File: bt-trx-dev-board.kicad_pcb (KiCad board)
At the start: 2 copper layers, 64.5 x 68 mm, 53 parts, among them J2 PTT_BUTTON, J3 AudioJack2, J4 PTT_SELECT, J5 RJ45, J6 ENABLE_PTT_IN, J7 I2C, SW1 SW_Push, U1 SILabs_WT32i, U2 LM1117-5.0, U3 Teensy3.2

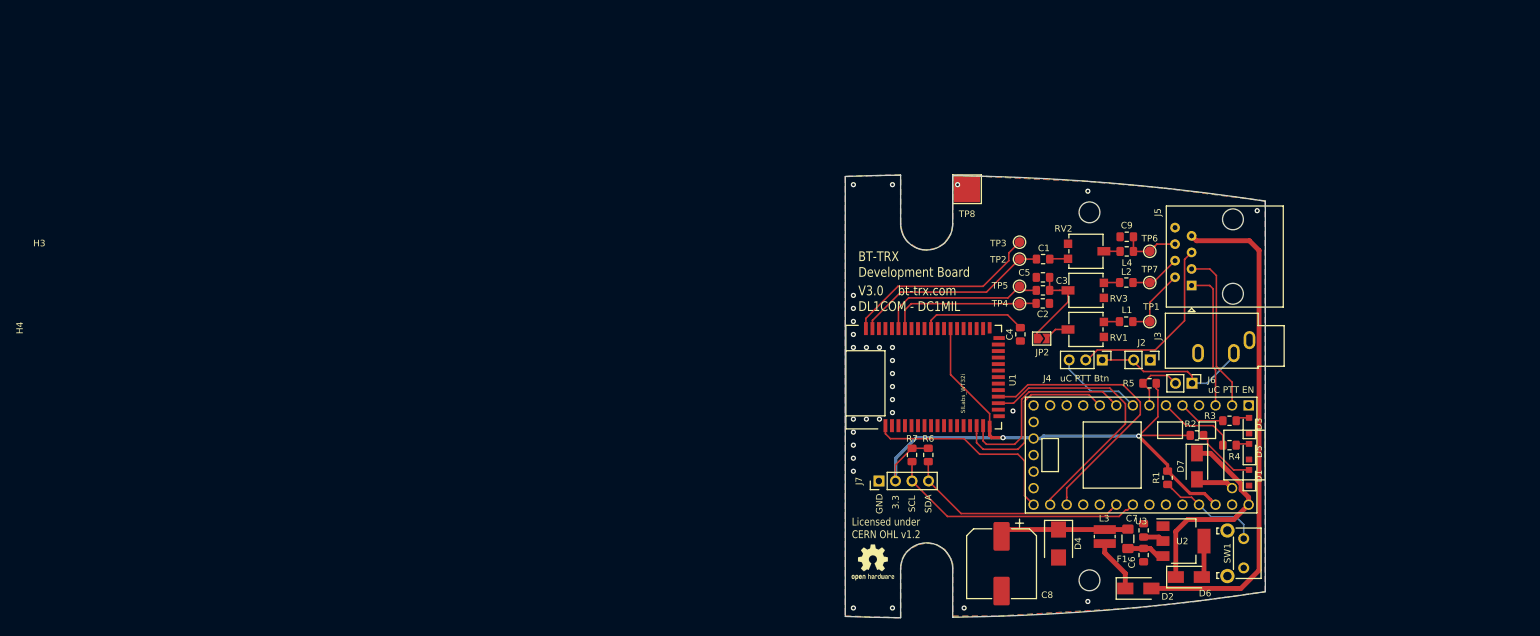
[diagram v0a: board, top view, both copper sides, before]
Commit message: Continued v4 [#1]
*removed all v3 stuff
* Resized board to max case size
* First deratsnesting
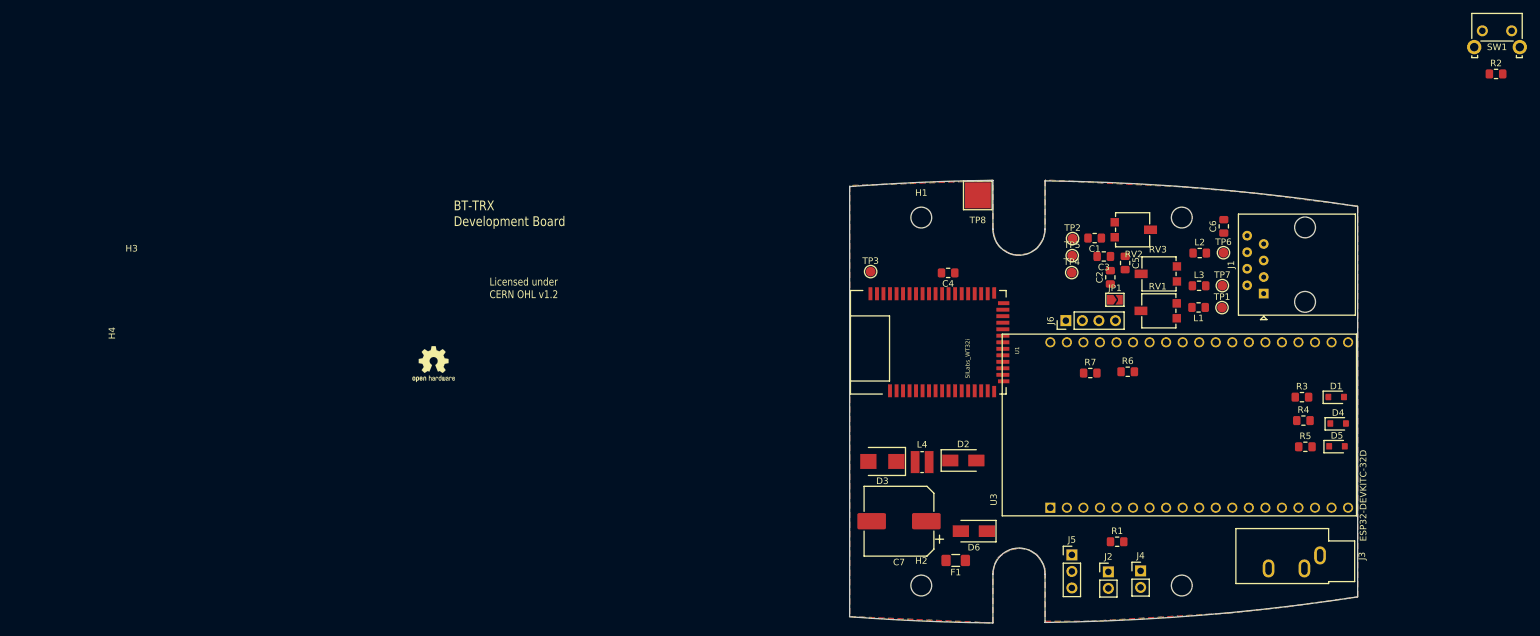
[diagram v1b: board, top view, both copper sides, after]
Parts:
- removed C8: 220uF, Capacitor_SMD:CP_Elec_10x10.5
- removed C9: 10nF, Capacitor_SMD:C_0805_2012Metric_Pad1.15x1.40mm_HandSolder
- removed D7: 1N5817, Diode_SMD:D_SMA
- removed J7: I2C, Connector_PinHeader_2.54mm:PinHeader_1x04_P2.54mm_Vertical
- removed JP2: AUDIO_B, Jumper:SolderJumper-2_P1.3mm_Open_TrianglePad1.0x1.5mm
- removed U2: LM1117-5.0, Package_TO_SOT_SMD:SOT-223-3_TabPin2
- added H1: MountingHole, MountingHole:MountingHole_3.2mm_M3_DIN965, F.Cu at (131.4, 71.0)
- added H2: MountingHole, MountingHole:MountingHole_3.2mm_M3_DIN965, F.Cu at (131.4, 127.5)
- added J1: RJ45, Connector_RJ:RJ45_Amphenol_54602-x08_Horizontal, F.Cu at (184.0, 82.7)
- added JP1: AUDIO_B, Jumper:SolderJumper-2_P1.3mm_Open_TrianglePad1.0x1.5mm, F.Cu at (161.2, 83.7)
- C6: value 100nF tantal -> 10nF
- C7: value 100nF tantal -> 220uF 25V; footprint Capacitor_SMD:C_0805_2012Metric_Pad1.15x1.40mm_HandSolder -> Capacitor_SMD:CP_Elec_10x10.5
- D3: value LED BLUE 2mA -> TVS 16V; footprint Kingbright:APA2107LSECK -> Diode_SMD:D_SMB
- D4: value TVS 16V -> LED BLUE 2mA; footprint Diode_SMD:D_SMB -> Kingbright:APA2107LSECK
- J4: value PTT_SELECT -> ENABLE_PTT_IN; footprint Connector_PinHeader_2.54mm:PinHeader_1x03_P2.54mm_Vertical -> Connector_PinHeader_2.54mm:PinHeader_1x02_P2.54mm_Vertical
- J5: value RJ45 -> PTT_SELECT; footprint Connector_RJ:RJ45_Amphenol_54602-x08_Horizontal -> Connector_PinHeader_2.54mm:PinHeader_1x03_P2.54mm_Vertical
- J6: value ENABLE_PTT_IN -> I2C; footprint Connector_PinHeader_2.54mm:PinHeader_1x02_P2.54mm_Vertical -> Connector_PinHeader_2.54mm:PinHeader_1x04_P2.54mm_Vertical
- L3: value 47uH, 390mA -> 100nH; footprint Inductor_SMD:L_Wuerth_MAPI-3020 -> Inductor_SMD:L_0805_2012Metric_Pad1.15x1.40mm_HandSolder
- L4: value 100nH -> 47uH, 390mA; footprint Inductor_SMD:L_0805_2012Metric_Pad1.15x1.40mm_HandSolder -> Inductor_SMD:L_Wuerth_MAPI-3020
- R2: value 2.2k -> 10k
- R3: value 820R -> 2.2k
- R5: value 10k -> 820R
- U3: value Teensy3.2 -> ESP32-DEVKITC-32D; footprint teensy:Teensy30_31_32_LC_stripped -> ESP32-DEVKITC-32D:MODULE_ESP32-DEVKITC-32D
- moved SW1 86.2 mm to (217.6, 42.4), turned to 0 degrees
- moved N1 74.0 mm to (56.5, 93.5)
- moved R2 72.0 mm to (219.7, 49.0)
- moved D3 56.6 mm to (125.5, 108.5), turned to 180 degrees
- moved C6 52.0 mm to (177.9, 72.4), turned to 90 degrees
- moved D4 46.7 mm to (195.4, 102.7), turned to 0 degrees
- moved J5 45.3 mm to (154.6, 122.8), turned to 0 degrees
- moved L4 45.1 mm to (131.6, 108.6)
- moved L3 41.1 mm to (174.1, 81.5), turned to 0 degrees
- moved C7 37.6 mm to (128.0, 117.7), turned to 180 degrees
- moved J3 34.8 mm to (192.7, 122.9)
- moved D6 33.7 mm to (139.5, 119.2), turned to 180 degrees
- moved D2 33.3 mm to (137.9, 108.3)
- moved R6 33.2 mm to (163.1, 94.7), turned to 0 degrees
- moved J2 33.2 mm to (160.2, 125.5), turned to 0 degrees
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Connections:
- C6 pad 1: Net-(C6-Pad1) -> /AUDIO_OUT
- D3 pad 1: GND -> Net-(C7-Pad1)
- D3 pad 2: Net-(D3-Pad2) -> GND
- D4 pad 1: Net-(C8-Pad1) -> GND
- D4 pad 2: GND -> Net-(D4-Pad2)
- D6 pad 2: Net-(C7-Pad1) -> Net-(D6-Pad2)
- F1 pad 1: Net-(C6-Pad1) -> Net-(D6-Pad2)
- F1 pad 2: Net-(C8-Pad1) -> Net-(C7-Pad1)
- J4 pad 2: /PTT -> /UC_PTT_IN
- J5 pad 1: /CAT_TX -> /PTT_BUTTON
- J5 pad 2: /AUDIO_IN_B -> /PTT
- J5 pad 3: /CAT_RX -> /UC_PTT_OUT
- J6 pad 1: /PTT_BUTTON -> GND
- J6 pad 2: /PTT_IN -> +3V3
- L2 pad 2: /AUDIO_IN_A -> /AUDIO_OUT
- L3 pad 1: Net-(C8-Pad1) -> Net-(L3-Pad1)
- L3 pad 2: Net-(D2-Pad1) -> /AUDIO_IN_A
- L4 pad 1: Net-(L4-Pad1) -> Net-(C7-Pad1)
- L4 pad 2: /AUDIO_OUT -> Net-(D2-Pad1)
- R1 pad 2: /Microcontroller/BTN0 -> /UC_PTT_IN
- R2 pad 2: Net-(D1-Pad2) -> /Microcontroller/BTN0
- R3 pad 1: /Microcontroller/LED0 -> +3V3
- R3 pad 2: Net-(D3-Pad2) -> Net-(D1-Pad2)
- R4 pad 1: /Microcontroller/LED1 -> /Microcontroller/LED0
- R4 pad 2: Net-(D5-Pad2) -> Net-(D4-Pad2)
- R5 pad 1: +3V3 -> /Microcontroller/LED1
- R5 pad 2: /PTT_IN -> Net-(D5-Pad2)
- RV2 pad 2: Net-(L4-Pad1) -> Net-(L2-Pad1)
- RV3 pad 1: Net-(L2-Pad1) -> Net-(L3-Pad1)
- U3 pad 1: GND -> +3V3
- U3 pad 10: /UART_UC_TX -> /Microcontroller/LED1
- U3 pad 14: (no net) -> GND
- U3 pad 16: +3V3 -> (no net)
- U3 pad 17: GND -> (no net)
- U3 pad 19: (no net) -> +5V
- U3 pad 2: /CAT_RX -> (no net)
- U3 pad 20: /WT32_ONOFF_FROM_UC -> GND
- U3 pad 21: /UART_UC_CTS -> /WT32_ONOFF_FROM_UC
- U3 pad 22: /UART_UC_RTS -> /Microcontroller/SCL
- U3 pad 26: /Microcontroller/SCL -> GND
- U3 pad 28: (no net) -> /UART_UC_CTS
- U3 pad 29: (no net) -> /UART_UC_RTS
- U3 pad 3: /CAT_TX -> (no net)
- U3 pad 30: /Microcontroller/BTN0 -> /UART_UC_TX
- U3 pad 31: +3V3 -> /UART_UC_RX
- U3 pad 32: GND -> /Microcontroller/BTN0
- U3 pad 33: +5V -> (no net)
- U3 pad 34: /Microcontroller/VUSB -> (no net)
- U3 pad 5: /Microcontroller/LED0 -> (no net)
- U3 pad 6: /Microcontroller/LED1 -> (no net)
- U3 pad 7: /PTT_IN -> /UC_PTT_IN
- U3 pad 8: /PTT_UC -> /UC_PTT_OUT
- U3 pad 9: /UART_UC_RX -> /Microcontroller/LED0
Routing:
- net +3V3: track 106.1 -> 0.00 mm, vias 2 -> 0
- net /V_IN: track 78.1 -> 0.00 mm
- net /UART_UC_RTS: track 44.1 -> 0.00 mm
- net /UART_UC_CTS: track 41.8 -> 0.00 mm
- net /Microcontroller/SCL: track 39.9 -> 0.00 mm
- net /Microcontroller/SDA: track 34.5 -> 0.00 mm
- net +5V: track 32.3 -> 0.00 mm
- net /WT32_ONOFF_FROM_UC: track 31.6 -> 0.00 mm
- net /SPK_LP: track 30.7 -> 0.00 mm
- net /UART_UC_RX: track 30.7 -> 0.00 mm
- net /SPK_LN: track 30.3 -> 0.00 mm
- net /UART_UC_TX: track 29.8 -> 0.00 mm
- net /PTT: track 28.7 -> 0.00 mm
- net /MIC_LN: track 25.9 -> 0.00 mm
- net /CAT_RX: track 25.2 -> 0.00 mm
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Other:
- board size 64.5 x 68 mm -> 78 x 68 mm
- board text removed: "3.3"
- board text removed: "GND"
- board text removed: "SCL"
- board text removed: "SDA"
- board text removed: "V3.0 bt-trx.com DL1COM - DC1MIL"
- board text removed: "uC PTT Btn"
- board text removed: "uC PTT EN"

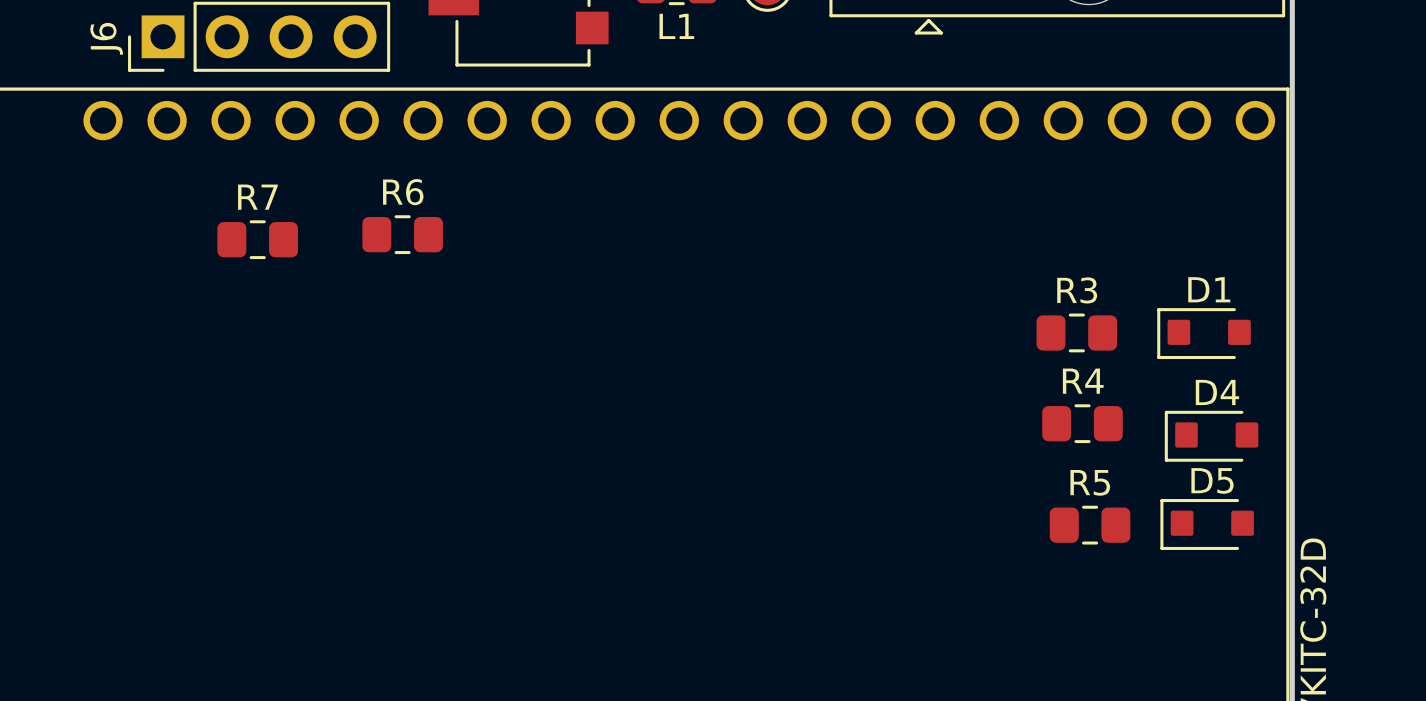
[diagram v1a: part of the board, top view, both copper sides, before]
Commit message: [#1] Refined Schematic
* Removed RTS CTS
* Added 15pF capacitator to audio IN+
* Removed PTT jumper
* Added pull-up jumper
* Added solder jmpr bypass to RV
* Changed button footprint to SMD version
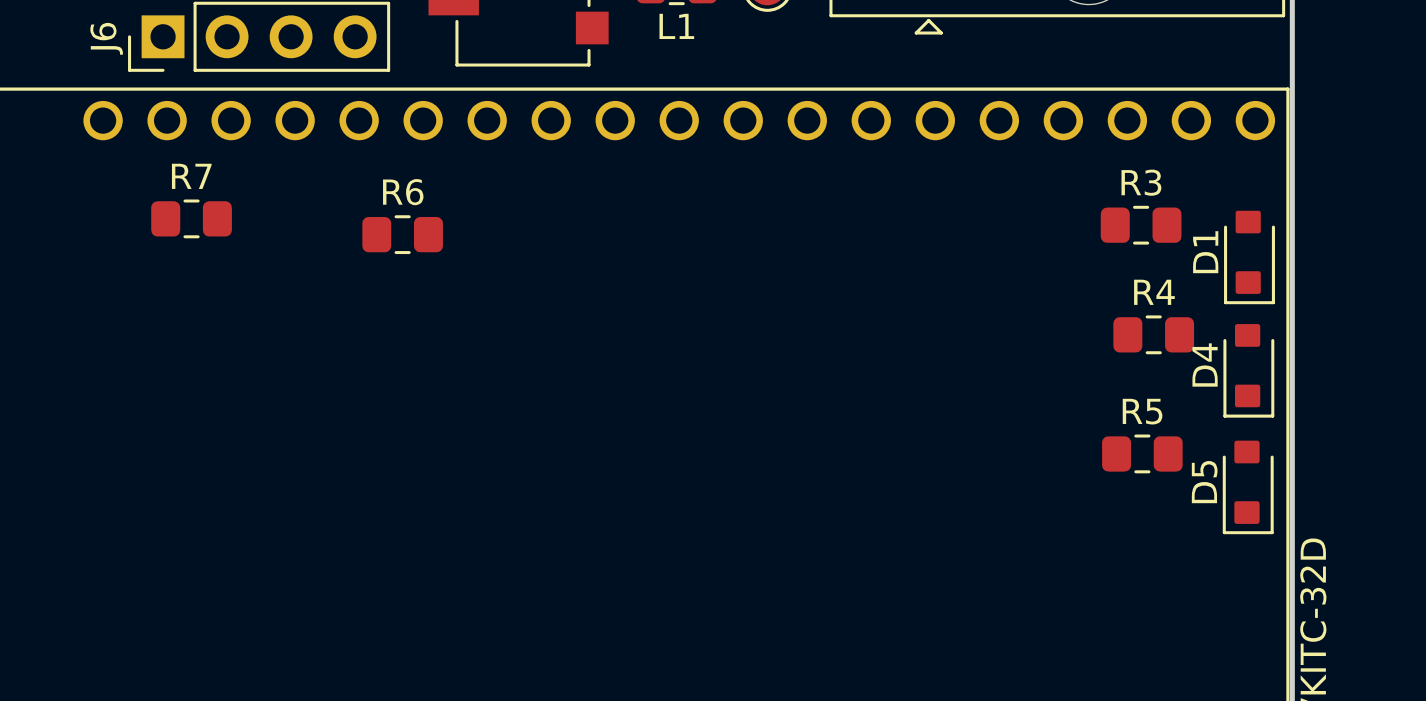
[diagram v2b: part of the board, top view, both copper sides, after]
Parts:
- moved R3 4.98 mm to (192.4, 94.3)
- moved R4 4.52 mm to (192.9, 98.7)
- moved D1 3.53 mm to (196.7, 95.4), turned to 90 degrees
- moved R5 3.51 mm to (192.5, 103.4)
- moved D4 3.01 mm to (196.7, 99.9), turned to 90 degrees
- moved R7 2.75 mm to (154.8, 94.1)
- moved D5 2.13 mm to (196.6, 104.5), turned to 90 degrees
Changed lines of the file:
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@@
   )
   (module Kingbright:APA2107LSECK (layer F.Cu)
-    (at 195.125 98.6)
+    (at 196.675 95.425 90)
     (descr "LED SMD 0805 (2012 Metric), square (rectangular) end terminal, IPC_7351 nominal, (Body size source: https://docs.google.com/spreadsheets/d/1BsfQQcO9C6DZCsRaXUlFlo91Tg2WpOkGARC1WS5S8t0/edit?usp=sharing), generated with kicad-footprint-generator")
     (tags diode)
     (attr smd)
-    (fp_text reference D1 (at 0 -1.65) (layer F.SilkS)
-      (effects (font (size 1 1) (thickness 0.15)))
-    )
-    (fp_text value "LED AMBER 2mA" (at 0 1.8) (layer F.Fab)
+    (fp_text reference D1 (at 0 -1.65 90) (layer F.SilkS)
+      (effects (font (size 1 1) (thickness 0.15)))
+    )
+    (fp_text value "LED AMBER 2mA" (at 0 1.8 90) (layer F.Fab)
       (effects (font (size 1 1) (thickness 0.15)))
     )
@@
     (fp_line (start 2 -0.9) (end 2 1) (layer F.CrtYd) (width 0.05))
     (fp_line (start 2 1) (end -2 1) (layer F.CrtYd) (width 0.05))
-    (fp_text user %R (at 0 0) (layer F.Fab)
+    (fp_text user %R (at 0 0 90) (layer F.Fab)
       (effects (font (size 0.5 0.5) (thickness 0.08)))
     )
-    (pad 1 smd roundrect (at -1.2 0) (size 0.9 1) (layers F.Cu F.Paste F.Mask) (roundrect_rratio 0.1)
-      (net 1 GND))
-    (pad 2 smd roundrect (at 1.2 0) (size 0.9 1) (layers F.Cu F.Paste F.Mask) (roundrect_rratio 0.1)
+    (pad 1 smd roundrect (at -1.2 0 90) (size 0.9 1) (layers F.Cu F.Paste F.Mask) (roundrect_rratio 0.1)
+      (net 1 GND))
+    (pad 2 smd roundrect (at 1.2 0 90) (size 0.9 1) (layers F.Cu F.Paste F.Mask) (roundrect_rratio 0.1)
       (net 29 "Net-(D1-Pad2)"))
     (model ${KISYS3DMOD}/LED_SMD.3dshapes/LED_0805_2012Metric.wrl
@@
   )
   (module Kingbright:APA2107LSECK (layer F.Cu)
-    (at 195.425 102.675)
+    (at 196.65 99.925 90)
     (descr "LED SMD 0805 (2012 Metric), square (rectangular) end terminal, IPC_7351 nominal, (Body size source: https://docs.google.com/spreadsheets/d/1BsfQQcO9C6DZCsRaXUlFlo91Tg2WpOkGARC1WS5S8t0/edit?usp=sharing), generated with kicad-footprint-generator")
     (tags diode)
     (attr smd)
-    (fp_text reference D4 (at 0 -1.65) (layer F.SilkS)
-      (effects (font (size 1 1) (thickness 0.15)))
-    )
-    (fp_text value "LED BLUE 2mA" (at 0 1.8) (layer F.Fab)
+    (fp_text reference D4 (at 0 -1.65 90) (layer F.SilkS)
+      (effects (font (size 1 1) (thickness 0.15)))
+    )
+    (fp_text value "LED BLUE 2mA" (at 0 1.8 90) (layer F.Fab)
       (effects (font (size 1 1) (thickness 0.15)))
     )
@@
     (fp_line (start 2 -0.9) (end 2 1) (layer F.CrtYd) (width 0.05))
     (fp_line (start 2 1) (end -2 1) (layer F.CrtYd) (width 0.05))
-    (fp_text user %R (at 0 0) (layer F.Fab)
+    (fp_text user %R (at 0 0 90) (layer F.Fab)
       (effects (font (size 0.5 0.5) (thickness 0.08)))
     )
-    (pad 1 smd roundrect (at -1.2 0) (size 0.9 1) (layers F.Cu F.Paste F.Mask) (roundrect_rratio 0.1)
-      (net 1 GND))
-    (pad 2 smd roundrect (at 1.2 0) (size 0.9 1) (layers F.Cu F.Paste F.Mask) (roundrect_rratio 0.1)
+    (pad 1 smd roundrect (at -1.2 0 90) (size 0.9 1) (layers F.Cu F.Paste F.Mask) (roundrect_rratio 0.1)
+      (net 1 GND))
+    (pad 2 smd roundrect (at 1.2 0 90) (size 0.9 1) (layers F.Cu F.Paste F.Mask) (roundrect_rratio 0.1)
       (net 33 "Net-(D4-Pad2)"))
     (model ${KISYS3DMOD}/LED_SMD.3dshapes/LED_0805_2012Metric.wrl
@@
   )
   (module Kingbright:APA2107LSECK (layer F.Cu)
-    (at 195.25 106.175)
+    (at 196.625 104.55 90)
     (descr "LED SMD 0805 (2012 Metric), square (rectangular) end terminal, IPC_7351 nominal, (Body size source: https://docs.google.com/spreadsheets/d/1BsfQQcO9C6DZCsRaXUlFlo91Tg2WpOkGARC1WS5S8t0/edit?usp=sharing), generated with kicad-footprint-generator")
     (tags diode)
     (attr smd)
-    (fp_text reference D5 (at 0 -1.65) (layer F.SilkS)
-      (effects (font (size 1 1) (thickness 0.15)))
-    )
-    (fp_text value "LED GREEN 2mA" (at 0 1.8) (layer F.Fab)
-      (effects (font (size 1 1) (thickness 0.15)))
-    )
-    (fp_text user %R (at 0 0) (layer F.Fab)
+    (fp_text reference D5 (at 0 -1.65 90) (layer F.SilkS)
+      (effects (font (size 1 1) (thickness 0.15)))
+    )
+    (fp_text value "LED GREEN 2mA" (at 0 1.8 90) (layer F.Fab)
+      (effects (font (size 1 1) (thickness 0.15)))
+    )
+    (fp_text user %R (at 0 0 90) (layer F.Fab)
       (effects (font (size 0.5 0.5) (thickness 0.08)))
     )
@@
     (fp_line (start -0.7 -0.6) (end -1 -0.3) (layer F.Fab) (width 0.1))
     (fp_line (start 1 -0.6) (end -0.7 -0.6) (layer F.Fab) (width 0.1))
-    (pad 2 smd roundrect (at 1.2 0) (size 0.9 1) (layers F.Cu F.Paste F.Mask) (roundrect_rratio 0.1)
+    (pad 2 smd roundrect (at 1.2 0 90) (size 0.9 1) (layers F.Cu F.Paste F.Mask) (roundrect_rratio 0.1)
       (net 27 "Net-(D5-Pad2)"))
-    (pad 1 smd roundrect (at -1.2 0) (size 0.9 1) (layers F.Cu F.Paste F.Mask) (roundrect_rratio 0.1)
+    (pad 1 smd roundrect (at -1.2 0 90) (size 0.9 1) (layers F.Cu F.Paste F.Mask) (roundrect_rratio 0.1)
       (net 1 GND))
     (model ${KISYS3DMOD}/LED_SMD.3dshapes/LED_0805_2012Metric.wrl
@@
   )
   (module Resistor_SMD:R_0805_2012Metric_Pad1.15x1.40mm_HandSolder (layer F.Cu)
-    (at 189.875 98.625)
+    (at 192.425 94.35)
     (descr "Resistor SMD 0805 (2012 Metric), square (rectangular) end terminal, IPC_7351 nominal with elongated pad for handsoldering. (Body size source: https://docs.google.com/spreadsheets/d/1BsfQQcO9C6DZCsRaXUlFlo91Tg2WpOkGARC1WS5S8t0/edit?usp=sharing), generated with kicad-footprint-generator")
     (tags "resistor handsolder")
@@
   )
   (module Resistor_SMD:R_0805_2012Metric_Pad1.15x1.40mm_HandSolder (layer F.Cu)
-    (at 190.1 102.225)
+    (at 192.925 98.7)
     (descr "Resistor SMD 0805 (2012 Metric), square (rectangular) end terminal, IPC_7351 nominal with elongated pad for handsoldering. (Body size source: https://docs.google.com/spreadsheets/d/1BsfQQcO9C6DZCsRaXUlFlo91Tg2WpOkGARC1WS5S8t0/edit?usp=sharing), generated with kicad-footprint-generator")
     (tags "resistor handsolder")
@@
   )
   (module Resistor_SMD:R_0805_2012Metric_Pad1.15x1.40mm_HandSolder (layer F.Cu)
-    (at 190.4 106.25)
+    (at 192.475 103.425)
     (descr "Resistor SMD 0805 (2012 Metric), square (rectangular) end terminal, IPC_7351 nominal with elongated pad for handsoldering. (Body size source: https://docs.google.com/spreadsheets/d/1BsfQQcO9C6DZCsRaXUlFlo91Tg2WpOkGARC1WS5S8t0/edit?usp=sharing), generated with kicad-footprint-generator")
     (tags "resistor handsolder")
@@
   )
   (module Resistor_SMD:R_0805_2012Metric_Pad1.15x1.40mm_HandSolder (layer F.Cu)
-    (at 157.375 94.925)
+    (at 154.75 94.1)
     (descr "Resistor SMD 0805 (2012 Metric), square (rectangular) end terminal, IPC_7351 nominal with elongated pad for handsoldering. (Body size source: https://docs.google.com/spreadsheets/d/1BsfQQcO9C6DZCsRaXUlFlo91Tg2WpOkGARC1WS5S8t0/edit?usp=sharing), generated with kicad-footprint-generator")
     (tags "resistor handsolder")
@@
     (connect_pads (clearance 0.2))
     (min_thickness 0.2)
-    (fill (arc_segments 16) (thermal_gap 0.2) (thermal_bridge_width 0.508))
+    (fill yes (arc_segments 16) (thermal_gap 0.2) (thermal_bridge_width 0.508))
     (polygon
       (pts
